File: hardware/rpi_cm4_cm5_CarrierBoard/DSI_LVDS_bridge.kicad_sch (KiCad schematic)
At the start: 25 parts, among them Q10 SSM3K56FS,LF, Q11 SSM3K56FS,LF, U15 SN65DSI84ZXHR, U16 SN74LVC1G125DBVR

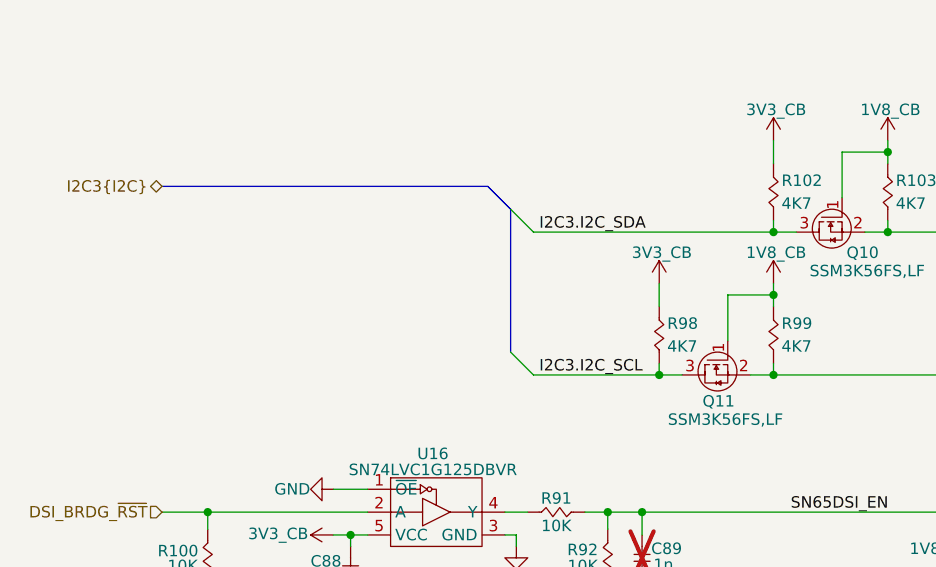
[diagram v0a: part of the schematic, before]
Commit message: Add test points on relevant signals Re-generate SCH_PDF Re-generate BOM Re-generate all gerbers and relevant PCB output files (still in review phase)
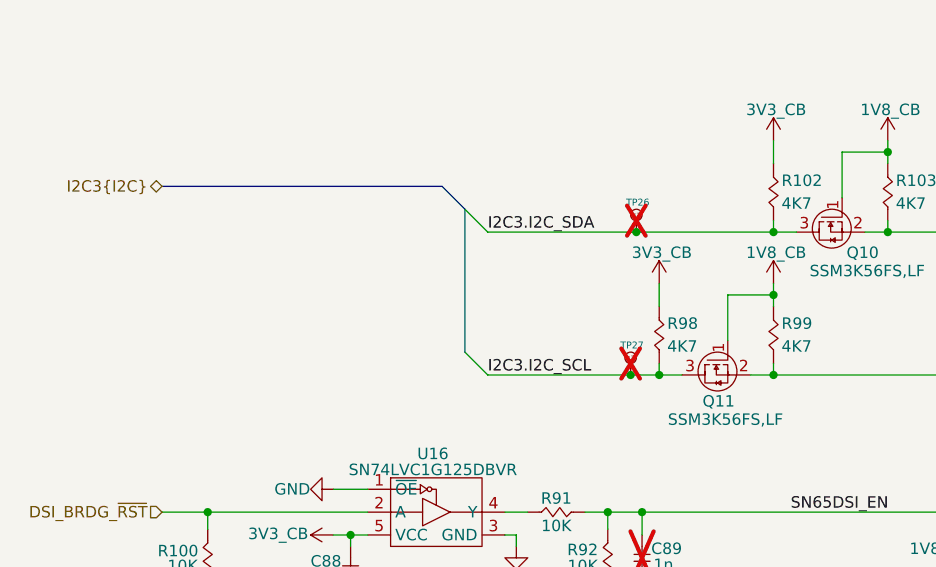
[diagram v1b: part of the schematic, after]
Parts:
- added TP26, TP27: 28 mils, footprint:SMT_TP_28_MILS, symbol KicadCompDb:Test Point/TP_00001
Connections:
- net I2C3.I2C_SCL: now also TP27.1
- net I2C3.I2C_SDA: now also TP26.1
